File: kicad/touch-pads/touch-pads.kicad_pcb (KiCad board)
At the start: 2 copper layers, 480 x 140 mm, 63 parts, among them J1 Conn_01x06_Socket, K1 Conn_01x01, K10 Conn_01x01, K11 Conn_01x01, K12 Conn_01x01, K13 Conn_01x01, K14 Conn_01x01, K15 Conn_01x01, K16 Conn_01x01, K17 Conn_01x01, K18 Conn_01x01, K19 Conn_01x01, K2 Conn_01x01, K20 Conn_01x01, K21 Conn_01x01, K22 Conn_01x01, K23 Conn_01x01, K24 Conn_01x01, K25 Conn_01x01, K26 Conn_01x01, K27 Conn_01x01, K28 Conn_01x01, K29 Conn_01x01, K3 Conn_01x01, K30 Conn_01x01, K31 Conn_01x01, K32 Conn_01x01, K4 Conn_01x01, K5 Conn_01x01, K6 Conn_01x01, K7 Conn_01x01, K8 Conn_01x01, K9 Conn_01x01, U1 CAP1188-1-CP-TR, U2 CAP1188-1-CP-TR, U3 CAP1188-1-CP-TR, U4 CAP1188-1-CP-TR

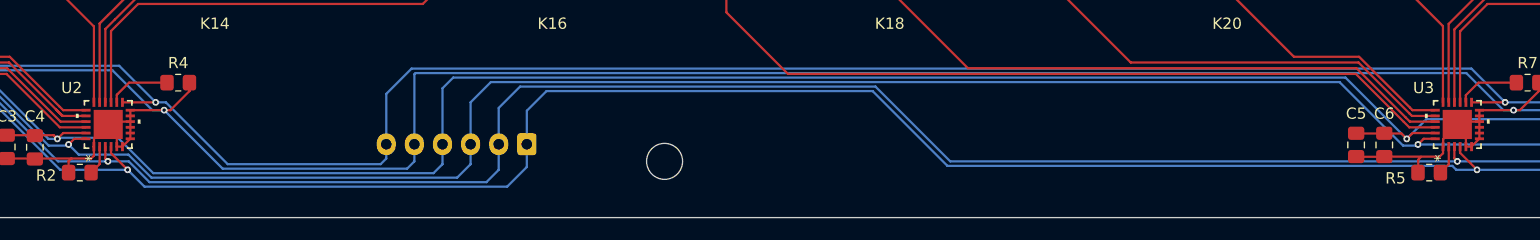
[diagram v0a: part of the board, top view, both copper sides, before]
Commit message: bom, update readme, move connector
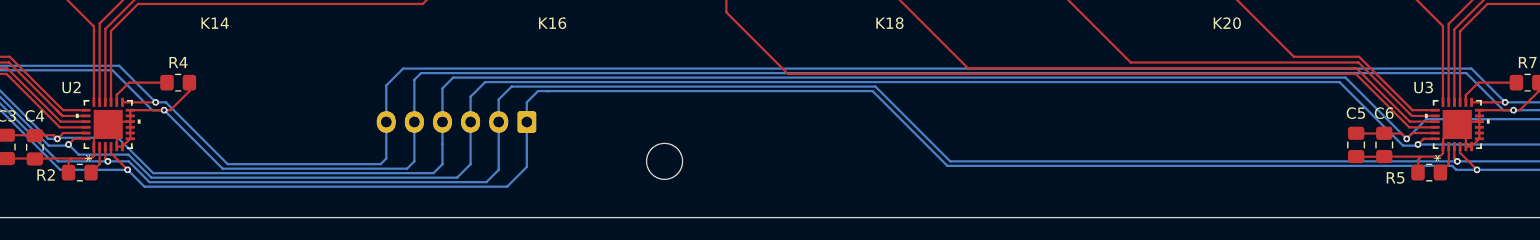
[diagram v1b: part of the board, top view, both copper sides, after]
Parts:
- moved J1 1.98 mm to (281.5, 256.5)
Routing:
- net SMCLK: track 394.5 -> 395.2 mm

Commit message: move common lib, cleanup tracks, logo
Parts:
- added G***: LOGO, Logo:Snep_Copper, B.Cu at (523.8, 258.0)
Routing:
- net Net-(K2-Pin_1): track 91.4 -> 79.4 mm
- net Net-(K10-Pin_1): track 91.4 -> 79.4 mm
- net Net-(K4-Pin_1): track 60.9 -> 48.9 mm
- net Net-(K12-Pin_1): track 60.9 -> 49.0 mm
